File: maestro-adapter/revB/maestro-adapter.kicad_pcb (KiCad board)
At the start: 2 copper layers, 34.2 x 72.9 mm, 46 parts, among them P1 CONN_01X07, P10 CONN_01X03, P11 CONN_01X03, P12 CONN_01X03, P13 CONN_01X03, P14 CONN_01X06, P15 CONN_01X06, P16 CONN_01X03, P2 CONN_01X03, P3 CONN_01X03, P4 CONN_01X03, P5 CONN_01X03, P6 CONN_01X03, P7 CONN_01X03, P8 CONN_01X03, P9 CONN_01X03, U1 Si866x, U2 Si866x

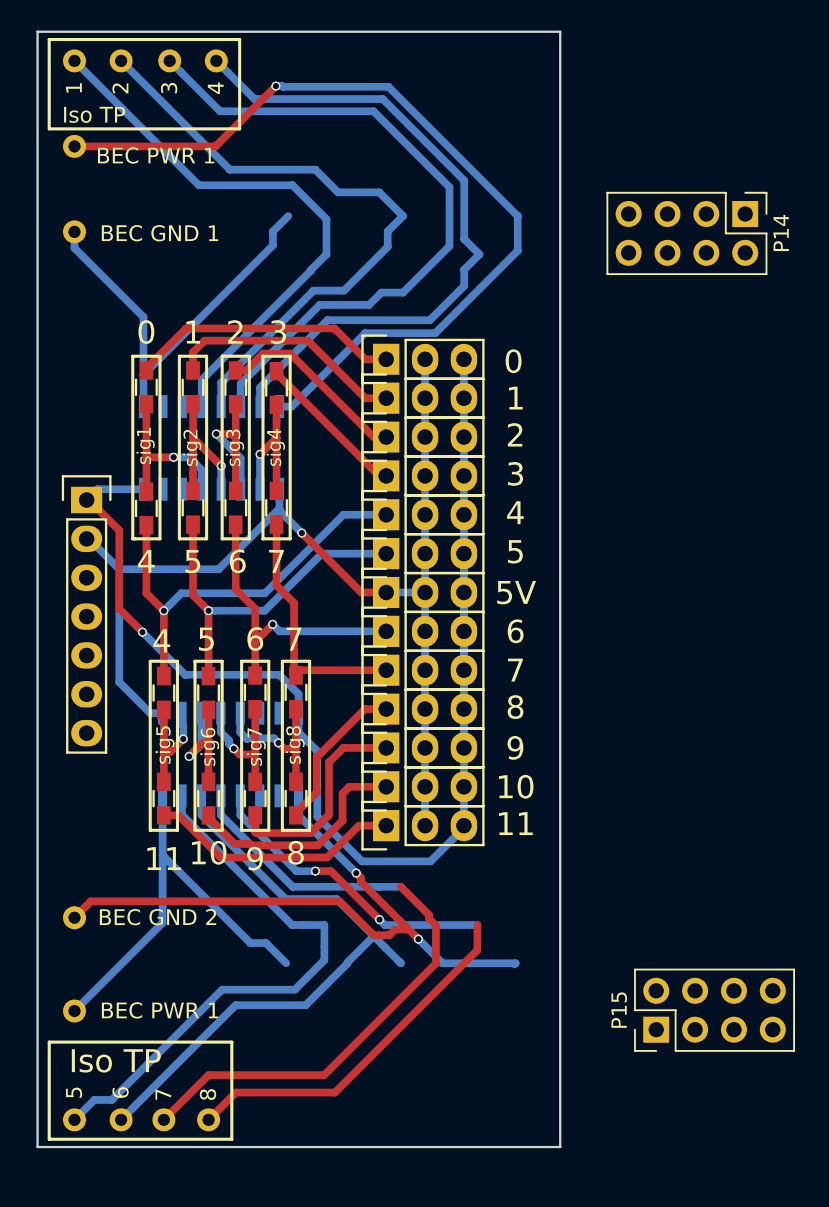
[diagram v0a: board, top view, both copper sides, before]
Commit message: Addition of updated maestro adapter
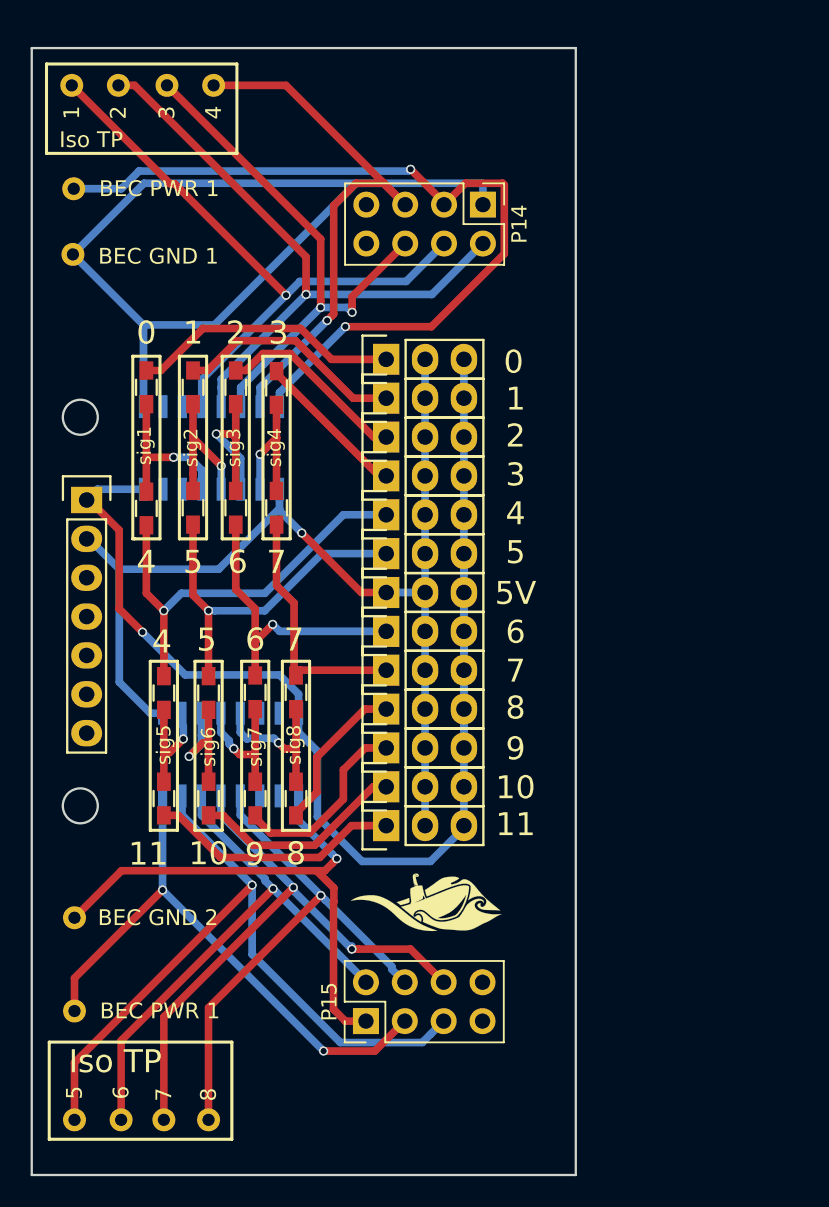
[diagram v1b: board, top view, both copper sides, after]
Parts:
- added G***: LOGO, robosub_footprints:robosub_logo-medium, F.Cu at (175.8, 118.0)
- moved P15 19.0 mm to (171.8, 125.6)
- moved P14 17.2 mm to (179.5, 72.3)
- moved W9 2.77 mm to (152.7, 71.2)
- moved W1 1.61 mm to (152.6, 64.5)
- moved W2 1.61 mm to (155.7, 64.5)
- moved W3 1.61 mm to (158.8, 64.5)
- moved W4 1.61 mm to (161.9, 64.5)
- moved W11 1.48 mm to (152.7, 75.5)
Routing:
- net /sig8_isolated: track 67.4 -> 34.5 mm, vias 2 -> 1
- net /bec_gnd_1: track 27.6 -> 59.7 mm
- net /sig7_isolated: track 19.1 -> 39.4 mm, vias 0 -> 2
- net /sig5_isolated: track 36.5 -> 47.9 mm, vias 0 -> 1
- net /bec_esc_2: track 27.4 -> 37.4 mm, vias 0 -> 2
- net /sig3_isolated: track 44.4 -> 35.4 mm, vias 0 -> 2
- net /sig4_isolated: track 44.5 -> 36.7 mm, vias 0 -> 1
- net /bec_gnd_2: track 43.1 -> 35.9 mm, vias 2 -> 1
- net /sig1_isolated: track 36.4 -> 41.0 mm, vias 0 -> 1
- net /sig6_isolated: track 40.0 -> 35.9 mm, vias 0 -> 1
- net /bec_esc_1: track 56.2 -> 54.2 mm, vias 1 -> 2
- net /sig7: track 14.0 -> 12.6 mm
- net /sig6: track 15.1 -> 14.0 mm
- net /sig2_isolated: track 41.2 -> 41.9 mm, vias 0 -> 1
- net /sig2: track 15.7 -> 15.0 mm
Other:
- board size 34.2 x 72.9 mm -> 35.6 x 73.7 mm

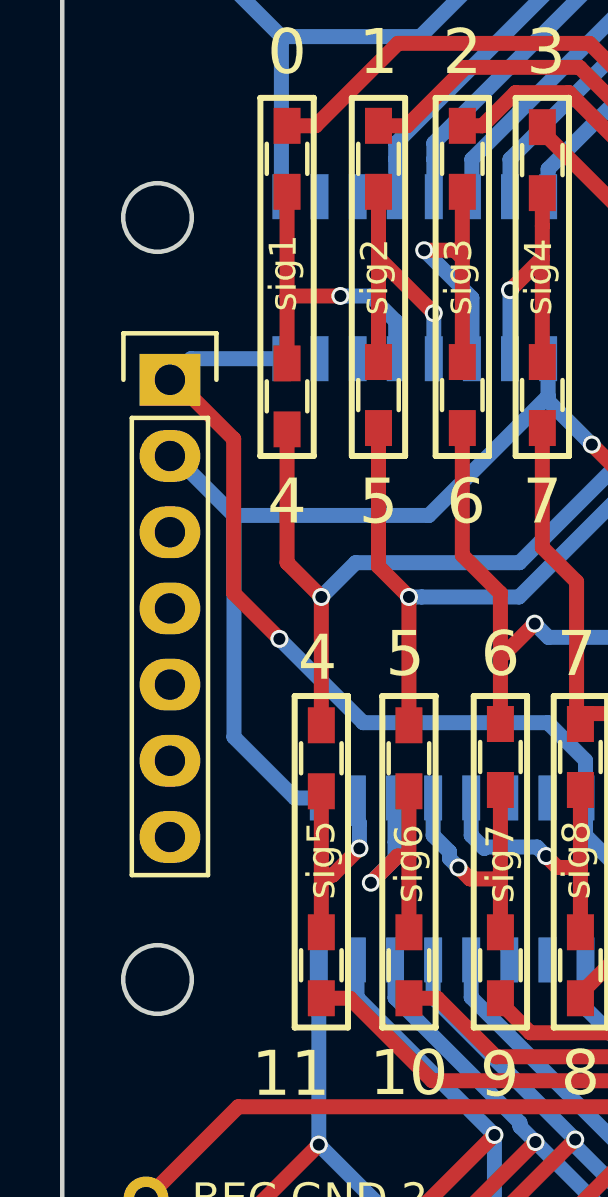
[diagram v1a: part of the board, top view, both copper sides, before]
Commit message: converted edge-cut mounting holes to KiCAD components
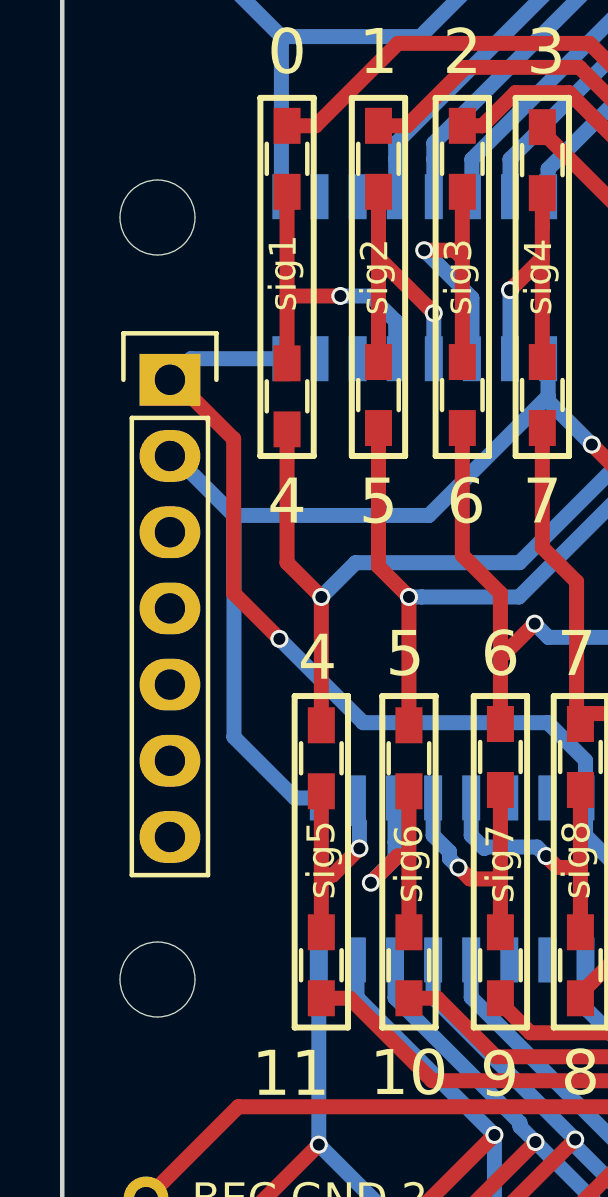
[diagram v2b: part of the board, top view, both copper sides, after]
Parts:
- added REF**: MountingHole_2.5mm, Mounting_Holes:MountingHole_2.5mm, F.Cu at (153.2, 111.6)
- added REF**: MountingHole_2.5mm, Mounting_Holes:MountingHole_2.5mm, F.Cu at (153.2, 86.2)
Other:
- outline, holes or cut-outs redrawn
- board text added: "Maestro Adapter Ryan Summers RS17 - RevB"
- board text removed: "Maestro Adapter Ryan Summers RS17"
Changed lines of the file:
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@@
     (area 149.911999 61.951799 185.622001 135.761801)
     (thickness 1.6)
-    (drawings 101)
+    (drawings 97)
     (tracks 334)
     (zones 0)
-    (modules 47)
+    (modules 49)
     (nets 35)
   )
@@
     (add_net /t4)
     (add_net GND)
+  )
+  (module Mounting_Holes:MountingHole_2.5mm (layer F.Cu)
+    (at 153.162 111.5568)
+    (descr "Mounting Hole 2.5mm, no annular")
+    (tags "mounting hole 2.5mm no annular")
+    (fp_text reference REF** (at 0 -3.5) (layer F.SilkS) hide
+      (effects (font (size 1 1) (thickness 0.15)))
+    )
+    (fp_text value MountingHole_2.5mm (at 0 3.5) (layer F.Fab)
+      (effects (font (size 1 1) (thickness 0.15)))
+    )
+    (fp_circle (center 0 0) (end 2.5 0) (layer Cmts.User) (width 0.15))
+    (fp_circle (center 0 0) (end 2.75 0) (layer F.CrtYd) (width 0.05))
+    (pad 1 np_thru_hole circle (at 0 0) (size 2.5 2.5) (drill 2.5) (layers *.Cu *.Mask))
   )
   (module robosub_footprints:robosub_logo-medium (layer F.Cu)
@@
     )
   )
-  (dimension 10.1092 (width 0.3) (layer Dwgs.User)
-    (gr_text "10.109 mm" (at 185.624082 130.669992 90) (layer Dwgs.User)
-      (effects (font (size 1.5 1.5) (thickness 0.3)))
-    )
-    (feature1 (pts (xy 179.491552 125.615392) (xy 186.974082 125.615392)))
-    (feature2 (pts (xy 179.491552 135.724592) (xy 186.974082 135.724592)))
-    (crossbar (pts (xy 184.274082 135.724592) (xy 184.274082 125.615392)))
-    (arrow1a (pts (xy 184.274082 125.615392) (xy 184.860503 126.741896)))
-    (arrow1b (pts (xy 184.274082 125.615392) (xy 183.687661 126.741896)))
-    (arrow2a (pts (xy 184.274082 135.724592) (xy 184.860503 134.598088)))
-    (arrow2b (pts (xy 184.274082 135.724592) (xy 183.687661 134.598088)))
-  )
-  (dimension 10.1092 (width 0.3) (layer Dwgs.User)
-    (gr_text "10.109 mm" (at 185.60893 67.2084 90) (layer Dwgs.User)
-      (effects (font (size 1.5 1.5) (thickness 0.3)))
-    )
-    (feature1 (pts (xy 179.4764 62.1538) (xy 186.95893 62.1538)))
-    (feature2 (pts (xy 179.4764 72.263) (xy 186.95893 72.263)))
-    (crossbar (pts (xy 184.25893 72.263) (xy 184.25893 62.1538)))
-    (arrow1a (pts (xy 184.25893 62.1538) (xy 184.845351 63.280304)))
-    (arrow1b (pts (xy 184.25893 62.1538) (xy 183.672509 63.280304)))
-    (arrow2a (pts (xy 184.25893 72.263) (xy 184.845351 71.136496)))
-    (arrow2b (pts (xy 184.25893 72.263) (xy 183.672509 71.136496)))
+  (module Mounting_Holes:MountingHole_2.5mm (layer F.Cu)
+    (at 153.162 86.1568)
+    (descr "Mounting Hole 2.5mm, no annular")
+    (tags "mounting hole 2.5mm no annular")
+    (fp_text reference REF** (at 0 -3.5) (layer F.SilkS) hide
+      (effects (font (size 1 1) (thickness 0.15)))
+    )
+    (fp_text value MountingHole_2.5mm (at 0 3.5) (layer F.Fab)
+      (effects (font (size 1 1) (thickness 0.15)))
+    )
+    (fp_circle (center 0 0) (end 2.5 0) (layer Cmts.User) (width 0.15))
+    (fp_circle (center 0 0) (end 2.75 0) (layer F.CrtYd) (width 0.05))
+    (pad 1 np_thru_hole circle (at 0 0) (size 2.5 2.5) (drill 2.5) (layers *.Cu *.Mask))
   )
   (gr_line (start 149.987 135.6868) (end 185.547 135.6868) (layer Edge.Cuts) (width 0.15))
@@
   (gr_line (start 185.547 62.0268) (end 149.987 62.0268) (layer Edge.Cuts) (width 0.15))
   (gr_line (start 149.987 62.0268) (end 149.987 135.6868) (layer Edge.Cuts) (width 0.15))
-  (gr_circle (center 153.162 86.1568) (end 153.162 87.2998) (layer Edge.Cuts) (width 0.15))
-  (gr_circle (center 153.162 111.5568) (end 153.162 112.6998) (layer Edge.Cuts) (width 0.15))
   (gr_line (start 157.734 102.108) (end 159.512 102.108) (layer F.SilkS) (width 0.2))
   (gr_line (start 157.734 113.157) (end 157.734 102.108) (layer F.SilkS) (width 0.2))
@@
     (effects (font (size 1.03 1.03) (thickness 0.1984)))
   )
-  (gr_text "Maestro Adapter\nRyan Summers\nRS17" (at 168.4782 80.5688) (layer B.SilkS)
+  (gr_text "Maestro Adapter\nRyan Summers\nRS17 - RevB" (at 183.4007 66.4718) (layer B.SilkS)
     (effects (font (size 1.5 1.5) (thickness 0.3)) (justify left mirror))
   )
